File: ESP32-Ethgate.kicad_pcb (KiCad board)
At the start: 2 copper layers, 76.2 x 38.1 mm, 54 parts, among them J1 USB_B_Micro, J2 HR911105A, Q1 UMH3N, U1 HT7233, U2 ESP32-WROOM-32U, U3 CH340C, U4 HT7233, U5 LAN8720A, U6 USBLC6-2SC6

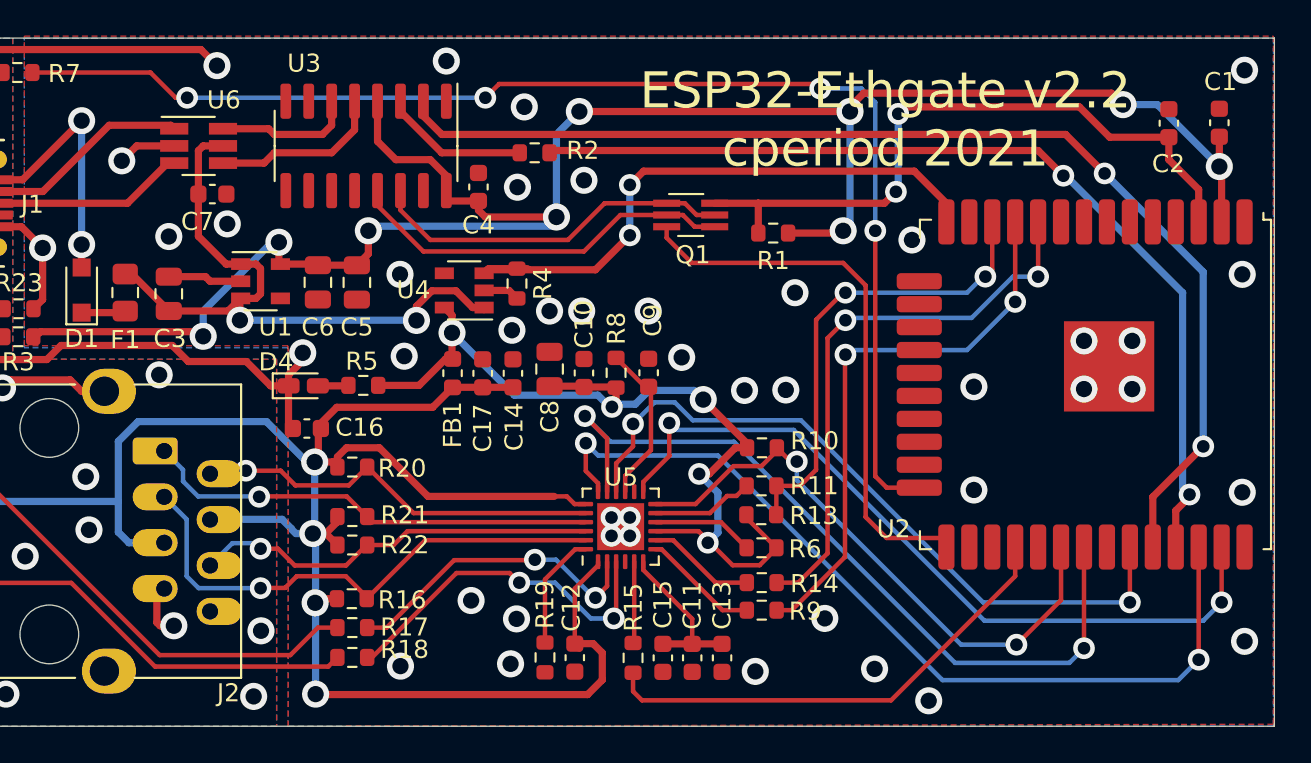
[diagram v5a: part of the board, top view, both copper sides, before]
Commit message: chop the ground plane up a bit less
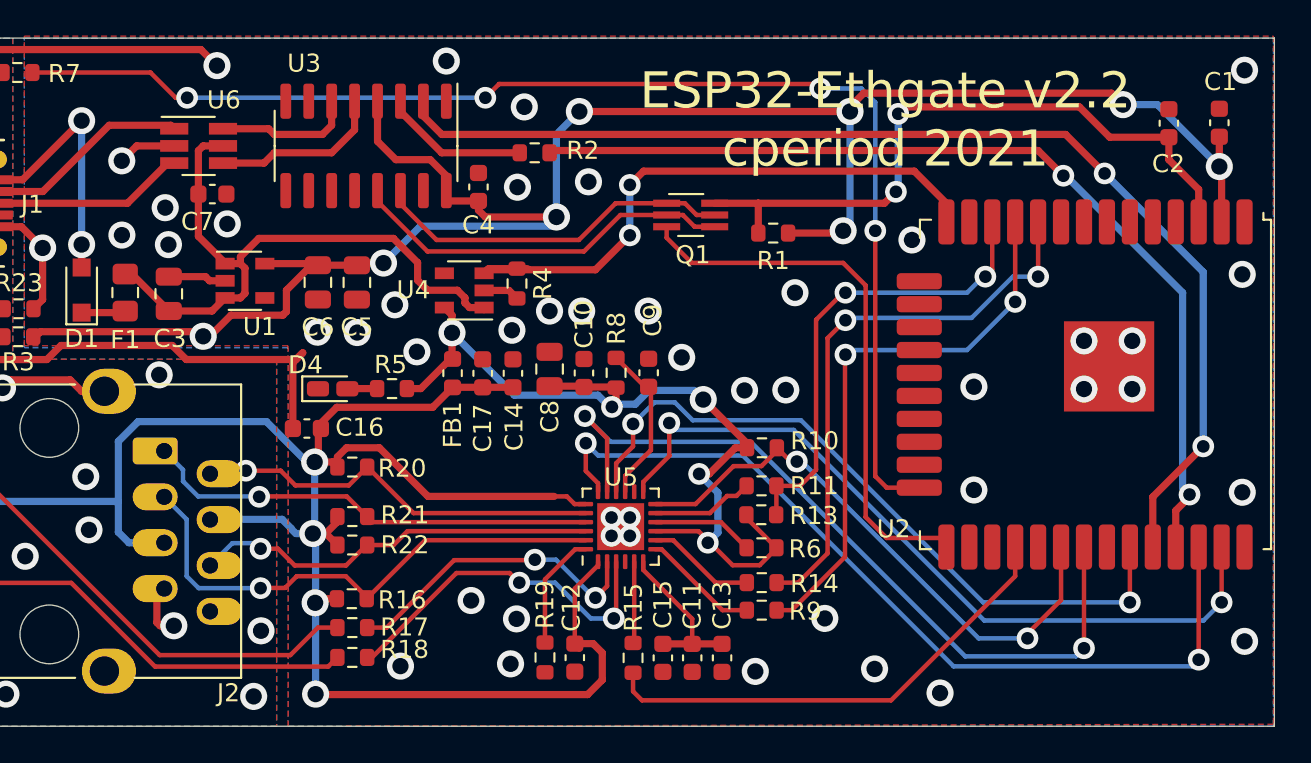
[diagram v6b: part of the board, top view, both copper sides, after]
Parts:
- moved D4 1.64 mm to (91.4, 80.4)
- moved R5 1.60 mm to (94.7, 80.4)
- moved U1 0.86 mm to (86.5, 74.4)
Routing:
- net /+3V3_LAN: track 51.0 -> 49.5 mm
- net +5V: track 36.9 -> 35.7 mm, vias 2 -> 0
- net /MDIO: track 33.4 -> 32.7 mm
- net GND: track 58.0 -> 57.2 mm, vias 43 -> 46
- net /TXD1: track 49.5 -> 48.9 mm
- net +3V3: track 109.5 -> 110.1 mm, vias 9 -> 8

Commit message: more layout tweaks
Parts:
- moved F1 11.0 mm to (80.3, 64.1), turned to 180 degrees
- moved D1 10.9 mm to (76.3, 64.1), turned to 180 degrees
- moved C14 6.15 mm to (95.2, 79.5)
- moved C17 6.15 mm to (93.5, 79.5)
- moved FB1 6.15 mm to (91.9, 79.5)
- moved D4 5.65 mm to (85.9, 78.9)
- moved R5 5.65 mm to (89.2, 78.8)
- moved U1 2.29 mm to (84.3, 73.9)
- moved C3 2.29 mm to (80.1, 74.6)
- moved C5 2.25 mm to (90.5, 73.9)
- moved C6 2.25 mm to (88.4, 73.9)
- moved R3 1.90 mm to (72.1, 77.6)
- moved R7 1.76 mm to (72.1, 62.8)
- moved C7 1.68 mm to (83.0, 69.6), turned to 180 degrees
- moved R1 1.67 mm to (116.0, 70.1)
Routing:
- net Net-(D1-Pad2): track 14.1 -> 6.62 mm, vias 2 -> 0
- net +3.3VA: track 121.2 -> 115.6 mm
- net /+3V3_LAN: track 49.5 -> 54.8 mm
- net GND: track 57.2 -> 52.8 mm, vias 46 -> 52
- net +3V3: track 110.1 -> 106.0 mm, vias 8 -> 9
- net +5V: track 35.7 -> 39.1 mm
- net Net-(D2-Pad2): track 4.32 -> 2.26 mm
- net Net-(D3-Pad2): track 4.65 -> 2.81 mm
- net /SLED: track 71.9 -> 73.7 mm
- net /EN: track 38.0 -> 37.0 mm
- net /IO0: track 30.5 -> 31.5 mm
- net Net-(D1-Pad1): track 2.45 -> 1.92 mm
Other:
- net class Default: via_drill 0.7 -> 0.6
- rule via_min_drill: 0.7 -> 0.6

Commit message: more tweaks
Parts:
- moved C10 7.42 mm to (98.0, 80.9), turned to 180 degrees
- moved Q1 5.62 mm to (105.6, 71.4)
- moved C8 5.58 mm to (97.8, 79.0), turned to 180 degrees
- moved U2 5.29 mm to (128.3, 80.0)
- moved C1 5.29 mm to (135.2, 65.5)
- moved C2 5.29 mm to (132.4, 65.5)
- moved C12 4.93 mm to (99.8, 95.3)
- moved R8 4.93 mm to (102.1, 79.5)
- moved C11 4.93 mm to (106.3, 95.3)
- moved C13 4.93 mm to (108.0, 95.3)
- moved C15 4.93 mm to (104.7, 95.3)
- moved C9 4.93 mm to (103.9, 79.5)
- moved R10 4.93 mm to (110.2, 83.7)
- moved R11 4.93 mm to (110.2, 85.8)
- moved R13 4.93 mm to (110.2, 87.4)
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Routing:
- net +3.3VA: track 115.6 -> 105.9 mm
- net /+3V3_LAN: track 54.8 -> 47.8 mm, vias 5 -> 4
- net +3V3: track 106.0 -> 99.2 mm
- net /ACTLED: track 19.8 -> 13.3 mm
- net /LINKLED: track 17.3 -> 11.4 mm
- net RTS: track 20.1 -> 14.2 mm
- net DTR: track 21.5 -> 15.7 mm
- net /SLED: track 73.7 -> 68.6 mm
- net /RXN: track 22.7 -> 17.7 mm
- net /RXP: track 29.5 -> 24.5 mm
- net /TXP: track 25.4 -> 20.5 mm
- net /TXN: track 22.8 -> 17.9 mm
- net /PHY_POWER: track 34.3 -> 29.7 mm
- net GND: track 52.8 -> 56.6 mm
- net /eRX: track 63.5 -> 59.9 mm
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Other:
- board size 76.2 x 38.1 mm -> 71.2 x 38.1 mm
